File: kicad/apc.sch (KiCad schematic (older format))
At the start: 13 parts, among them U101 LM556

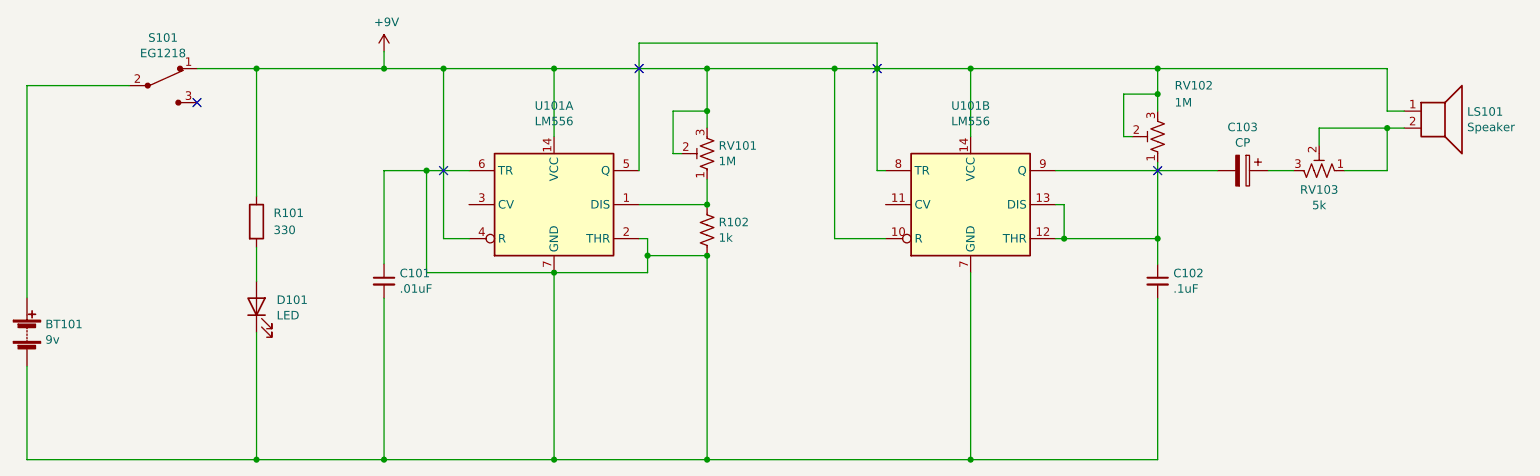
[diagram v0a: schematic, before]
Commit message: PCB revisions:
* Add voltage regulator to POLY_555
* Ditch hitch
* Reorder switches+circuits left to right
* Carve out room for battery
* Mark # 555s
* Label wired pins better

APC updates:

* Fix ground error
* Reverse volume pot direction
* Swap timing cap footprint
* Add stress relief hole for battery wires
* Widen speaker pins
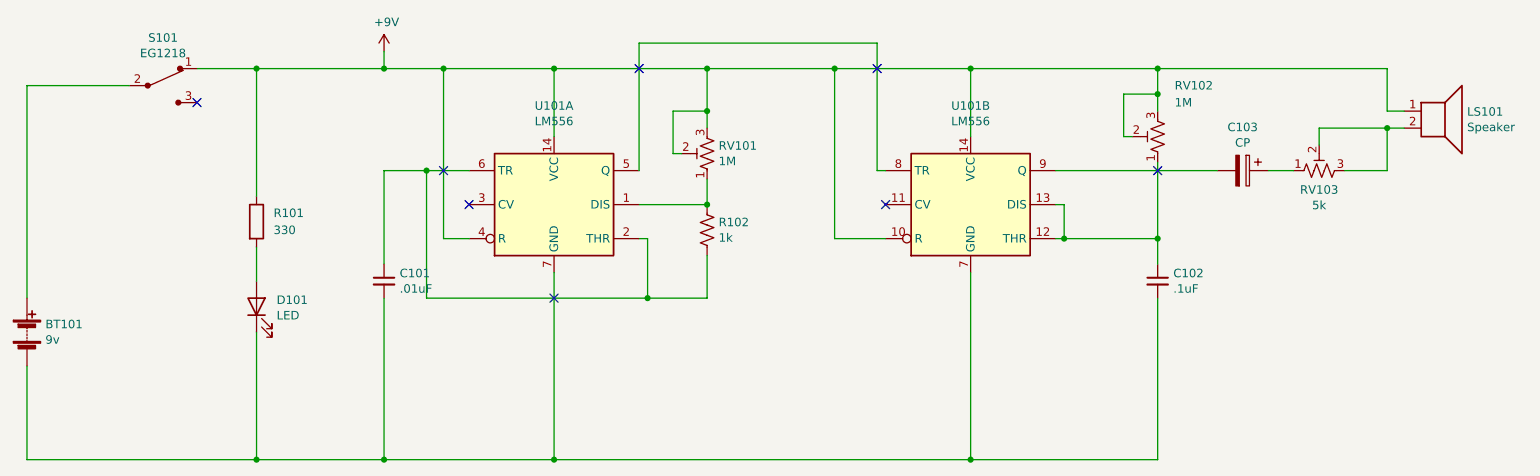
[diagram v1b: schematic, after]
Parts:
- C103: footprint Capacitor_THT:CP_Radial_D8.0mm_P3.50mm -> Capacitor_THT:CP_Radial_D4.0mm_P2.00mm
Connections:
- net +9V: no longer U101.5 (Q), U101.8 (TR)
- net at BT101.2 (-), C101.2, C102.2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: no longer C101.1, R102.2, U101.2 (THR), U101.6 (TR)
- net at LS101.2, RV103.2: now also RV103.3; no longer RV103.1
- net at C103.1: now also RV103.1; no longer RV103.3
- new net: C101.1, R102.2, U101.2 (THR), U101.6 (TR)
- new net: U101.5 (Q), U101.8 (TR)
- no-connect marks 5 -> 8
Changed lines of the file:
@@
 	-1   0    0    1
-$EndComp
-$Comp
-L Timer:LM556 U101
-U 1 1 5F4726A4
-P 4150 3500
-F 0 "U101" H 4150 4081 50  0000 C CNN
-F 1 "LM556" H 4150 3990 50  0000 C CNN
-F 2 "Package_DIP:DIP-14_W7.62mm_LongPads" H 4150 3500 50  0001 C CNN
-F 3 "http://www.ti.com/lit/ds/symlink/lm556.pdf" H 4150 3500 50  0001 C CNN
-	1    4150 3500
-	1    0    0    -1
 $EndComp
 Wire Wire Line
@@
 	4650 3700 4700 3700
 Wire Wire Line
-	4700 3700 4700 3800
-Wire Wire Line
-	4700 3800 5050 3800
-Wire Wire Line
-	3650 3300 3400 3300
-Wire Wire Line
-	5050 5000 5050 3800
-Connection ~ 5050 3800
-Wire Wire Line
-	5050 5000 6600 5000
-Connection ~ 5050 5000
-Wire Wire Line
-	4650 3300 4650 2550
-Wire Wire Line
 	4650 2550 6050 2550
-Wire Wire Line
-	6050 2550 6050 2700
 Wire Wire Line
 	6050 3300 6100 3300
@@
 	3500 2700 4150 2700
 NoConn ~ 3500 3300
-NoConn ~ 4650 2700
-NoConn ~ 6050 2700
-Connection ~ 6050 2700
-Wire Wire Line
-	6050 2700 6600 2700
-Wire Wire Line
-	6050 2700 6050 3300
 Connection ~ 5050 2700
 $Comp
@@
 	7700 3700 7700 3850
 Connection ~ 7150 3700
-$Comp
-L Device:R_POT_TRIM_US RV102
-U 1 1 5F48C811
-P 7700 3100
-F 0 "RV102" H 7600 2800 50  0000 R CNN
-F 1 "1M" H 7600 2900 50  0000 R CNN
-F 2 "Potentiometer_THT:Potentiometer_Piher_PT-6-V_Vertical" H 7700 3100 50  0001 C CNN
-F 3 "~" H 7700 3100 50  0001 C CNN
-	1    7700 3100
-	-1   0    0    1
-$EndComp
-Wire Wire Line
-	7550 3100 7500 3100
-Wire Wire Line
-	7500 3100 7500 2850
 Wire Wire Line
 	6600 2700 7700 2700
-Wire Wire Line
-	7700 2700 7700 2850
-Connection ~ 6600 2700
-Wire Wire Line
-	7700 2850 7500 2850
-Connection ~ 7700 2850
-Wire Wire Line
-	7700 2850 7700 2950
 Wire Wire Line
 	7700 3250 7700 3700
@@
 	1    0    0    -1
 $EndComp
-$Comp
-L Device:CP C103
-U 1 1 5F496041
-P 8200 3300
-F 0 "C103" V 7945 3300 50  0000 C CNN
-F 1 "CP" V 8036 3300 50  0000 C CNN
-F 2 "Capacitor_THT:CP_Radial_D8.0mm_P3.50mm" H 8238 3150 50  0001 C CNN
-F 3 "~" H 8200 3300 50  0001 C CNN
-	1    8200 3300
-	0    1    1    0
-$EndComp
 Wire Wire Line
 	7700 2700 9050 2700
@@
 	8050 3300 7100 3300
 NoConn ~ 7700 3300
-$Comp
-L Device:R_POT_TRIM_US RV103
-U 1 1 5F4918D3
-P 8650 3300
-F 0 "RV103" V 8537 3300 50  0000 C CNN
-F 1 "5k" V 8446 3300 50  0000 C CNN
-F 2 "Potentiometer_THT:Potentiometer_Piher_PT-6-V_Vertical" H 8650 3300 50  0001 C CNN
-F 3 "~" H 8650 3300 50  0001 C CNN
-	1    8650 3300
-	0    1    -1   0
-$EndComp
-Wire Wire Line
-	9050 3050 8650 3050
-Wire Wire Line
-	8650 3050 8650 3150
-Connection ~ 9050 3050
-Wire Wire Line
-	8350 3300 8500 3300
-Wire Wire Line
-	8800 3300 9050 3300
 Wire Wire Line
 	5800 3700 5800 2700
-Connection ~ 5800 2700
-Wire Wire Line
-	5800 2700 6050 2700
 Wire Wire Line
 	3150 5000 4150 5000
-Wire Wire Line
-	4150 3900 4150 5000
 Connection ~ 4150 5000
-Wire Wire Line
-	4150 5000 5050 5000
 Wire Wire Line
 	6600 3900 6600 5000
 Connection ~ 6600 5000
-Wire Wire Line
-	3400 3300 3400 3900
-Wire Wire Line
-	3400 3900 4150 3900
-Wire Wire Line
-	4700 3900 4700 3800
-Connection ~ 3400 3300
-Wire Wire Line
-	3400 3300 3150 3300
-Connection ~ 4150 3900
-Wire Wire Line
-	4150 3900 4700 3900
-Connection ~ 4700 3800
 $Comp
 L Timer:LM556 U101
@@
 Wire Wire Line
 	6600 5000 7700 5000
+Wire Wire Line
+	4150 3900 4150 5000
+$Comp
+L Timer:LM556 U101
+U 1 1 5F4726A4
+P 4150 3500
+F 0 "U101" H 4150 4081 50  0000 C CNN
+F 1 "LM556" H 4150 3990 50  0000 C CNN
+F 2 "Package_DIP:DIP-14_W7.62mm_LongPads" H 4150 3500 50  0001 C CNN
+F 3 "http://www.ti.com/lit/ds/symlink/lm556.pdf" H 4150 3500 50  0001 C CNN
+	1    4150 3500
+	1    0    0    -1
+$EndComp
+NoConn ~ 4150 4050
+Wire Wire Line
+	4150 5000 6600 5000
+Wire Wire Line
+	5050 3800 5050 4050
+Wire Wire Line
+	5050 4050 4700 4050
+Wire Wire Line
+	3650 3300 3400 3300
+Wire Wire Line
+	3400 3300 3150 3300
+Connection ~ 3400 3300
+Wire Wire Line
+	3400 3300 3400 4050
+Connection ~ 4700 4050
+Wire Wire Line
+	4700 4050 3400 4050
+Wire Wire Line
+	4700 3700 4700 4050
+NoConn ~ 6100 3500
+NoConn ~ 3650 3500
+Wire Wire Line
+	5800 2700 6600 2700
+Connection ~ 5800 2700
+Connection ~ 6600 2700
+Wire Wire Line
+	4650 3300 4650 2550
+Wire Wire Line
+	6050 3300 6050 2550
+NoConn ~ 6050 2700
+Wire Wire Line
+	7550 3100 7500 3100
+$Comp
+L Device:R_POT_TRIM_US RV102
+U 1 1 5F48C811
+P 7700 3100
+F 0 "RV102" H 7600 2800 50  0000 R CNN
+F 1 "1M" H 7600 2900 50  0000 R CNN
+F 2 "Potentiometer_THT:Potentiometer_Piher_PT-6-V_Vertical" H 7700 3100 50  0001 C CNN
+F 3 "~" H 7700 3100 50  0001 C CNN
+	1    7700 3100
+	-1   0    0    1
+$EndComp
+Wire Wire Line
+	7500 3100 7500 2850
+NoConn ~ 4650 2700
+Wire Wire Line
+	7700 2850 7700 2950
+Wire Wire Line
+	7700 2700 7700 2850
+Connection ~ 7700 2850
+Wire Wire Line
+	7700 2850 7500 2850
+$Comp
+L Device:CP C103
+U 1 1 5F496041
+P 8200 3300
+F 0 "C103" V 7945 3300 50  0000 C CNN
+F 1 "CP" V 8036 3300 50  0000 C CNN
+F 2 "Capacitor_THT:CP_Radial_D4.0mm_P2.00mm" H 8238 3150 50  0001 C CNN
+F 3 "~" H 8200 3300 50  0001 C CNN
+	1    8200 3300
+	0    1    1    0
+$EndComp
+$Comp
+L Device:R_POT_TRIM_US RV103
+U 1 1 5F4918D3
+P 8650 3300
+F 0 "RV103" V 8537 3300 50  0000 C CNN
+F 1 "5k" V 8446 3300 50  0000 C CNN
+F 2 "Potentiometer_THT:Potentiometer_Piher_PT-6-V_Vertical" H 8650 3300 50  0001 C CNN
+F 3 "~" H 8650 3300 50  0001 C CNN
+	1    8650 3300
+	0    -1   -1   0
+$EndComp
+Wire Wire Line
+	8350 3300 8500 3300
+Wire Wire Line
+	8800 3300 9050 3300
+Wire Wire Line
+	9050 3050 8650 3050
+Wire Wire Line
+	8650 3050 8650 3150
+Connection ~ 9050 3050
 $EndSCHEMATC

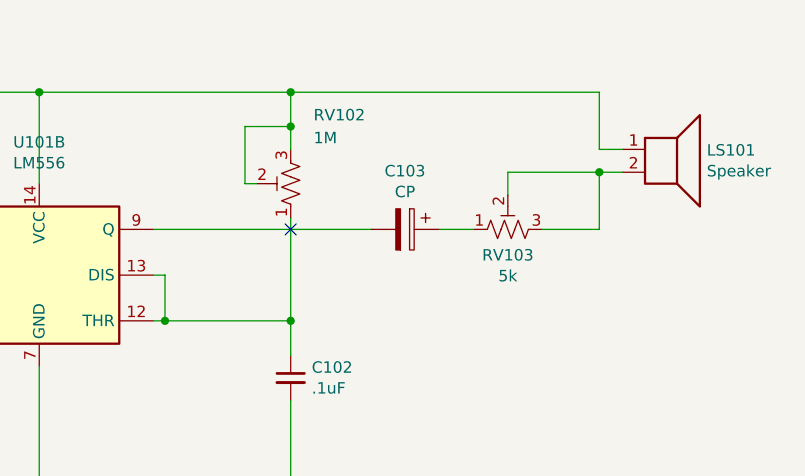
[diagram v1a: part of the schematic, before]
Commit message: Assign C103 value
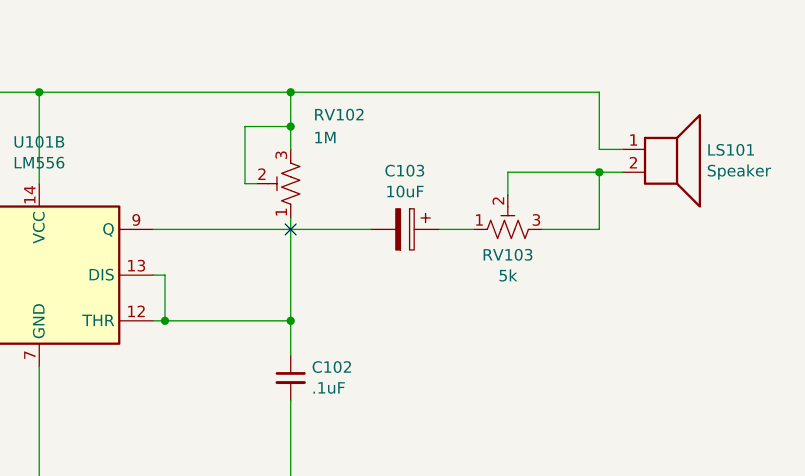
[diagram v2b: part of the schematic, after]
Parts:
- C103: value CP -> 10uF
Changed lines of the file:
@@
 P 8200 3300
 F 0 "C103" V 7945 3300 50  0000 C CNN
-F 1 "CP" V 8036 3300 50  0000 C CNN
+F 1 "10uF" V 8036 3300 50  0000 C CNN
 F 2 "Capacitor_THT:CP_Radial_D4.0mm_P2.00mm" H 8238 3150 50  0001 C CNN
 F 3 "~" H 8200 3300 50  0001 C CNN

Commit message: Upgrade APC pots and re-route
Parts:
- RV101, RV102: footprint Potentiometer_THT:Potentiometer_Piher_PT-6-V_Vertical -> Potentiometer_THT:Potentiometer_Bourns_PTV09A-2_Single_Horizontal
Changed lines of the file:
@@
 F 0 "RV101" H 4982 3154 50  0000 R CNN
 F 1 "1M" H 4982 3245 50  0000 R CNN
-F 2 "Potentiometer_THT:Potentiometer_Piher_PT-6-V_Vertical" H 5050 3200 50  0001 C CNN
+F 2 "Potentiometer_THT:Potentiometer_Bourns_PTV09A-2_Single_Horizontal" H 5050 3200 50  0001 C CNN
 F 3 "~" H 5050 3200 50  0001 C CNN
 	1    5050 3200
@@
 F 0 "RV102" H 7600 2800 50  0000 R CNN
 F 1 "1M" H 7600 2900 50  0000 R CNN
-F 2 "Potentiometer_THT:Potentiometer_Piher_PT-6-V_Vertical" H 7700 3100 50  0001 C CNN
+F 2 "Potentiometer_THT:Potentiometer_Bourns_PTV09A-2_Single_Horizontal" H 7700 3100 50  0001 C CNN
 F 3 "~" H 7700 3100 50  0001 C CNN
 	1    7700 3100

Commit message: Update APC pot footprints in schematic to match PCB
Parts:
- RV101, RV102: footprint Potentiometer_THT:Potentiometer_Bourns_PTV09A-2_Single_Horizontal -> Potentiometer_THT:Potentiometer_Bourns_PTV09A-1_Single_Vertical
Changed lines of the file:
@@
 F 0 "RV101" H 4982 3154 50  0000 R CNN
 F 1 "1M" H 4982 3245 50  0000 R CNN
-F 2 "Potentiometer_THT:Potentiometer_Bourns_PTV09A-2_Single_Horizontal" H 5050 3200 50  0001 C CNN
+F 2 "Potentiometer_THT:Potentiometer_Bourns_PTV09A-1_Single_Vertical" H 5050 3200 50  0001 C CNN
 F 3 "~" H 5050 3200 50  0001 C CNN
 	1    5050 3200
@@
 F 0 "RV102" H 7600 2800 50  0000 R CNN
 F 1 "1M" H 7600 2900 50  0000 R CNN
-F 2 "Potentiometer_THT:Potentiometer_Bourns_PTV09A-2_Single_Horizontal" H 7700 3100 50  0001 C CNN
+F 2 "Potentiometer_THT:Potentiometer_Bourns_PTV09A-1_Single_Vertical" H 7700 3100 50  0001 C CNN
 F 3 "~" H 7700 3100 50  0001 C CNN
 	1    7700 3100

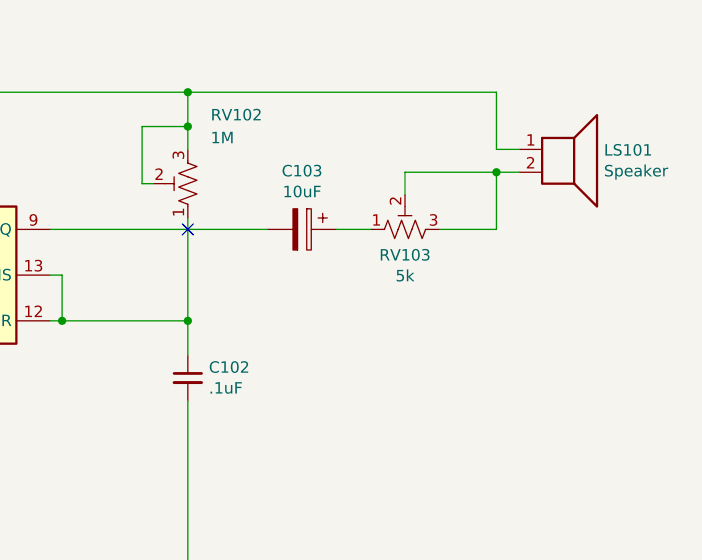
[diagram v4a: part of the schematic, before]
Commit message: Update APC vol from 5k to 1k
Cuz that's what I got!
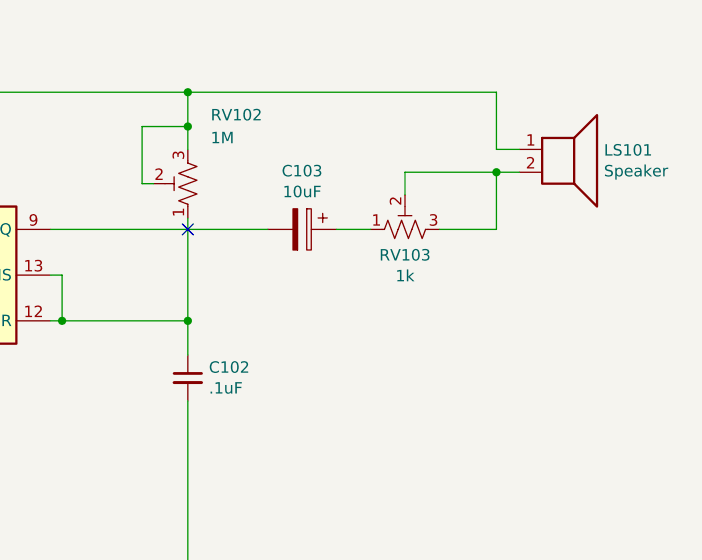
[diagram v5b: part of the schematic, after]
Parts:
- RV103: value 5k -> 1k
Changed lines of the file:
@@
 P 8650 3300
 F 0 "RV103" V 8537 3300 50  0000 C CNN
-F 1 "5k" V 8446 3300 50  0000 C CNN
+F 1 "1k" V 8446 3300 50  0000 C CNN
 F 2 "Potentiometer_THT:Potentiometer_Piher_PT-6-V_Vertical" H 8650 3300 50  0001 C CNN
 F 3 "~" H 8650 3300 50  0001 C CNN
